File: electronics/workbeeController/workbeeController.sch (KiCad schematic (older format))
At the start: 90 parts, among them J1 24V, J10 LIMIT Y2, J11 LIMIT Z, J12 ESTOP, J13 IN A, J14 IN B, J15 IN C, J16 IN D, J17 PROBE, J18 OUT_A, J19 OUT_B, J2 SR_OUT_EXT, J20 OUT_C, J21 OUT_D, J22 OUT_E, J23 OUT_F, J24 OUT_G, J25 OUT_H, J26 OUT_I, J27 OUT_J, J28 OUT_K, J29 OUT_L, J3 SR_IN_EXT, J30 OUT_M, J31 OUT_N, J32 OUT_O, J33 OUT_P, J34 RS485, J4 Conn_01x03_Male, J5 GND, J6 3.3v, J7 IN, J8 LIMIT X, J9 LIMIT Y1, U1 74HC595, U10 PC817, U11 PC817, U12 PC817, U13 PC817, U14 PC817, U15 PC817, U16 PC817, U2 74HC595, U3 TTGO_TDisplay, U4 Buck, U5 74HC165, U6 SP3485EN, U7 PC817, U8 PC817, U9 PC817

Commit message: Schematic updates
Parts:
- removed J4: Conn_01x03_Male, symbol Connector:Conn_01x03_Male
- added C?: 100uF, symbol Device:CP_Small
- added D?: 24V (Yellow), symbol Device:LED_Small
- added D?: 5V (Blue), symbol Device:LED_Small
- added D?: 3.3V (Green), symbol Device:LED_Small
- added J4: PULSE, symbol Connector:Screw_Terminal_01x03
- added R?: 2.2k, symbol Device:R_Small
- added R? (x2): 220, symbol Device:R_Small
- added U17: LevelShifterModule, symbol LevelShifterModule:LevelShifterModule
- U6: value SP3485EN -> SP485EN
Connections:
- net +24V: now also D?.2 (A)
- net +3V3: now also D?.2 (A), U17.3 (LV); no longer C4.2, R30.1, U6.8 (VCC)
- net +5V: now also C4.2, R30.1, U6.8 (VCC), C?.1, D?.2 (A), J4.2 (Pin_2), U17.10 (HV)
- net GND: now also C?.2, J4.3 (Pin_3), R?.2, R?.2, R?.2, U17.4 (GND), U17.9 (GND)
- net INT_PROBE: now also U3.23 (GPIO36); no longer U3.15 (GPIO27)
- net RS485_DI: now also U17.11 (HV2); no longer U3.19 (GPIO32)
- net RS485_RO: now also U17.12 (HV1); no longer U3.20 (GPIO39)
- net RS485_RTS: now also U17.8 (HV3); no longer U3.18 (GPIO33)
- net SR_IN_LATCH: now also U3.15 (GPIO27); no longer U3.23 (GPIO36)
- net PULSE renamed INT_PULSE
- net INT_PULSE: now also U17.6 (LV4)
- new net: D?.1 (K), R?.1 (x3)
- new net EXT_PULSE: J4.1 (Pin_1), U17.7 (HV4)
- new net RS485_DI_3V3: U17.2 (LV2), U3.19 (GPIO32)
- new net RS485_RO_3V3: U17.1 (LV1), U3.20 (GPIO39)
- new net RS485_RTS_3V3: U17.5 (LV3), U3.18 (GPIO33)
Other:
- note added: "Power"
- moved on the sheet: C3, C4, D1, F1, J1, J3, J34, JP1, R30, R31, R32, U3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

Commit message: Initial schematic and footprints complete
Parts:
- added H1, H2, H3, H4, H5: MountingHole_Pad, MountingHole:MountingHole_4.3mm_M4_ISO7380_Pad, symbol Mechanical:MountingHole_Pad
- added J35: 24V, Connector_PinHeader_2.54mm:PinHeader_1x04_P2.54mm_Vertical, symbol Connector:Conn_01x04_Female
- added J36: 5V, Connector_PinHeader_2.54mm:PinHeader_1x04_P2.54mm_Vertical, symbol Connector:Conn_01x04_Female
- added J37: 3.3V, Connector_PinHeader_2.54mm:PinHeader_1x04_P2.54mm_Vertical, symbol Connector:Conn_01x04_Female
- added J38: GND, Connector_PinHeader_2.54mm:PinHeader_1x04_P2.54mm_Vertical, symbol Connector:Conn_01x04_Female
- C1, C2, C3, C4: footprint (none) -> Capacitor_THT:C_Disc_D5.0mm_W2.5mm_P2.50mm
- C5: renamed from C?; footprint (none) -> Capacitor_THT:CP_Radial_D8.0mm_P3.50mm
- D1, D2: footprint (none) -> Diode_THT:D_DO-41_SOD81_P7.62mm_Horizontal
- D3, D4, D5: renamed from D?; footprint (none) -> LED_THT:LED_D3.0mm
- F1: footprint (none) -> Fuse:Fuse_1206_3216Metric_Pad1.42x1.75mm_HandSolder
- J1, J17, J18, J19, J20, J21, J22, J23, J24, J25, J26, J27, J28, J29, J30, J31, J32, J33: footprint (none) -> ScrewTerminal:057-EB21A-02-D
- J10: value LIMIT Y2 -> IN C; footprint (none) -> ScrewTerminal:057-EB21A-02-D
- J11: value LIMIT Z -> IN D; footprint (none) -> ScrewTerminal:057-EB21A-02-D
- J12: value ESTOP -> IN E; footprint (none) -> ScrewTerminal:057-EB21A-02-D
- J13: value IN A -> IN F; footprint (none) -> ScrewTerminal:057-EB21A-02-D
- J14: value IN B -> IN G; footprint (none) -> ScrewTerminal:057-EB21A-02-D
- J15: value IN C -> IN H; footprint (none) -> ScrewTerminal:057-EB21A-02-D
- J16: value IN D -> ESTOP; footprint (none) -> ScrewTerminal:057-EB21A-02-D
- J2, J3: footprint (none) -> Connector_PinHeader_2.54mm:PinHeader_1x05_P2.54mm_Vertical
- J34: footprint (none) -> RS485:RS485Module
- J4: footprint (none) -> Connector_PinHeader_2.54mm:PinHeader_1x03_P2.54mm_Vertical; symbol Connector:Screw_Terminal_01x03 -> Connector:Conn_01x03_Male
- J5, J6: footprint (none) -> Connector_PinHeader_2.54mm:PinHeader_1x04_P2.54mm_Vertical
- J7: value IN -> GPIO; footprint (none) -> Connector_PinHeader_2.54mm:PinHeader_1x04_P2.54mm_Vertical
- J8: value LIMIT X -> IN A; footprint (none) -> ScrewTerminal:057-EB21A-02-D
- J9: value LIMIT Y1 -> IN B; footprint (none) -> ScrewTerminal:057-EB21A-02-D
- JP1: footprint (none) -> Jumper:SolderJumper-2_P1.3mm_Bridged_Pad1.0x1.5mm
- R1, R10, R11, R12, R13, R14, R15, R16, R17, R18, R19, R2, R20, R21, R22, R23, R24, R25, R26, R27, R28, R29, R3, R30, R31, R32, R4, R5, R6, R7, R8, R9: footprint (none) -> Resistor_THT:R_Axial_DIN0207_L6.3mm_D2.5mm_P7.62mm_Horizontal
- R33, R34, R35: renamed from R?; footprint (none) -> Resistor_THT:R_Axial_DIN0207_L6.3mm_D2.5mm_P7.62mm_Horizontal
- U1, U2: footprint (none) -> Package_DIP:DIP-16_W7.62mm
- U17: footprint (none) -> LevelShifterModule:LevelShifterModule
- U3: footprint (none) -> ESP32:T-DISPLAY
- U4: footprint (none) -> Buck:BuckModule
- U5: footprint MODULE -> Package_DIP:DIP-16_W7.62mm
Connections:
- net EXT_LIMIT_X is gone; now on net EXT_IN_A: J8.2 (Pin_2), U7.1
- net EXT_LIMIT_Y1 is gone; now on net EXT_IN_B: J9.2 (Pin_2), U8.1
- net EXT_LIMIT_Y2 is gone; now on net EXT_IN_C: J10.2 (Pin_2), U9.1
- net EXT_LIMIT_Z is gone; now on net EXT_IN_D: J11.2 (Pin_2), U10.1
- net +24V: now also J35.1 (Pin_1), J35.2 (Pin_2), J35.3 (Pin_3), J35.4 (Pin_4)
- net +3V3: now also J37.1 (Pin_1), J37.2 (Pin_2), J37.3 (Pin_3), J37.4 (Pin_4)
- net +5V: now also J36.1 (Pin_1), J36.2 (Pin_2), J36.3 (Pin_3), J36.4 (Pin_4)
- net EXT_ESTOP: now also J16.2 (Pin_2); no longer J12.2 (Pin_2)
- net EXT_IN_A: no longer J13.2 (Pin_2), U12.1
- net EXT_IN_B: no longer J14.2 (Pin_2), U13.1
- net EXT_IN_C: no longer J15.2 (Pin_2), U14.1
- net EXT_IN_D: no longer J16.2 (Pin_2), U15.1
- net GND: now also J38.1 (Pin_1), J38.2 (Pin_2), J38.3 (Pin_3), J38.4 (Pin_4)
- net INT_IN_A: now also R11.1, U7.4; no longer R16.1, U12.4
- net INT_IN_B: now also R12.1, U8.4; no longer R17.1, U13.4
- net INT_IN_C: now also R13.1, U9.4; no longer R18.1, U14.4
- net INT_IN_D: now also R14.1, U10.4; no longer R19.1, U15.4
- net INT_IN_E: now also R16.1, U12.4; no longer J7.1 (Pin_1)
- net INT_IN_F: now also R17.1, U13.4; no longer J7.2 (Pin_2)
- net INT_IN_G: now also R18.1, U14.4; no longer J7.3 (Pin_3)
- net INT_IN_H: now also R19.1, U15.4; no longer J7.4 (Pin_4)
- removed net INT_LIMIT_X: R11.1, U3.5 (GPIO17), U7.4
- removed net INT_LIMIT_Y1: R12.1, U3.3 (GPIO21), U8.4
- removed net INT_LIMIT_Y2: R13.1, U3.4 (GPIO22), U9.4
- removed net INT_LIMIT_Z: R14.1, U10.4, U3.6 (GPIO2)
- new net EXT_IN_E: J12.2 (Pin_2), U12.1
- new net EXT_IN_F: J13.2 (Pin_2), U13.1
- new net EXT_IN_G: J14.2 (Pin_2), U14.1
- new net EXT_IN_H: J15.2 (Pin_2), U15.1
- new net Earth_Protective: H1.1, H2.1, H3.1, H4.1, H5.1
- new net GPIO_17: J7.2 (Pin_2), U3.5 (GPIO17)
- new net GPIO_2: J7.1 (Pin_1), U3.6 (GPIO2)
- new net GPIO_21: J7.4 (Pin_4), U3.3 (GPIO21)
- new net GPIO_22: J7.3 (Pin_3), U3.4 (GPIO22)
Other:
- note added: "24V input connections"
- note added: "24V isolation"
- note added: "Accessory power"
- note added: "I/O Shift Registers"
- note added: "Input"
- note added: "LEDs"
- note added: "Low voltage I/O connections"
- note added: "MCU"
- note added: "Mechanical"
- note added: "Output"
- note added: "RS485 / 5V interface"
- moved on the sheet: C1, C2, C4, D3, D4, D5, J10, J11, J12, J13, J14, J15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

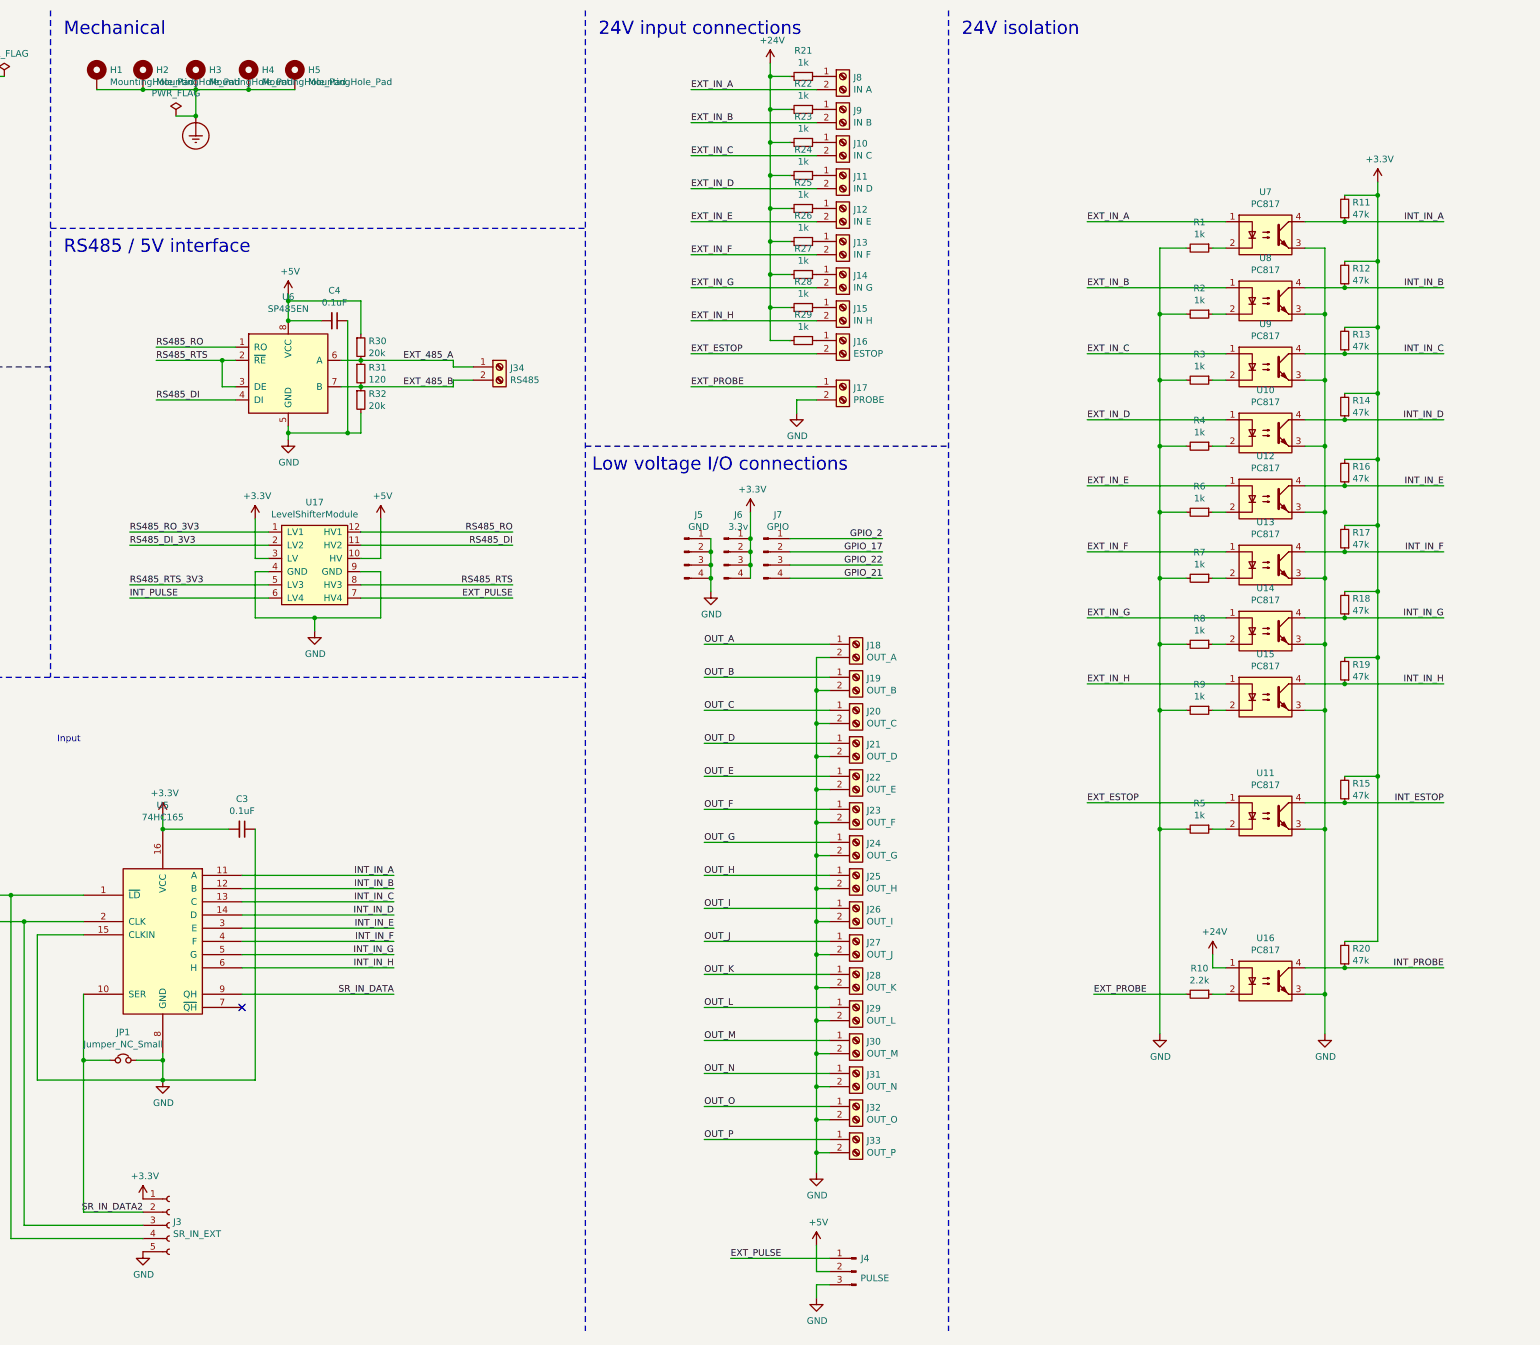
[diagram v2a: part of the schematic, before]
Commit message: Change to pin headers, start PCB
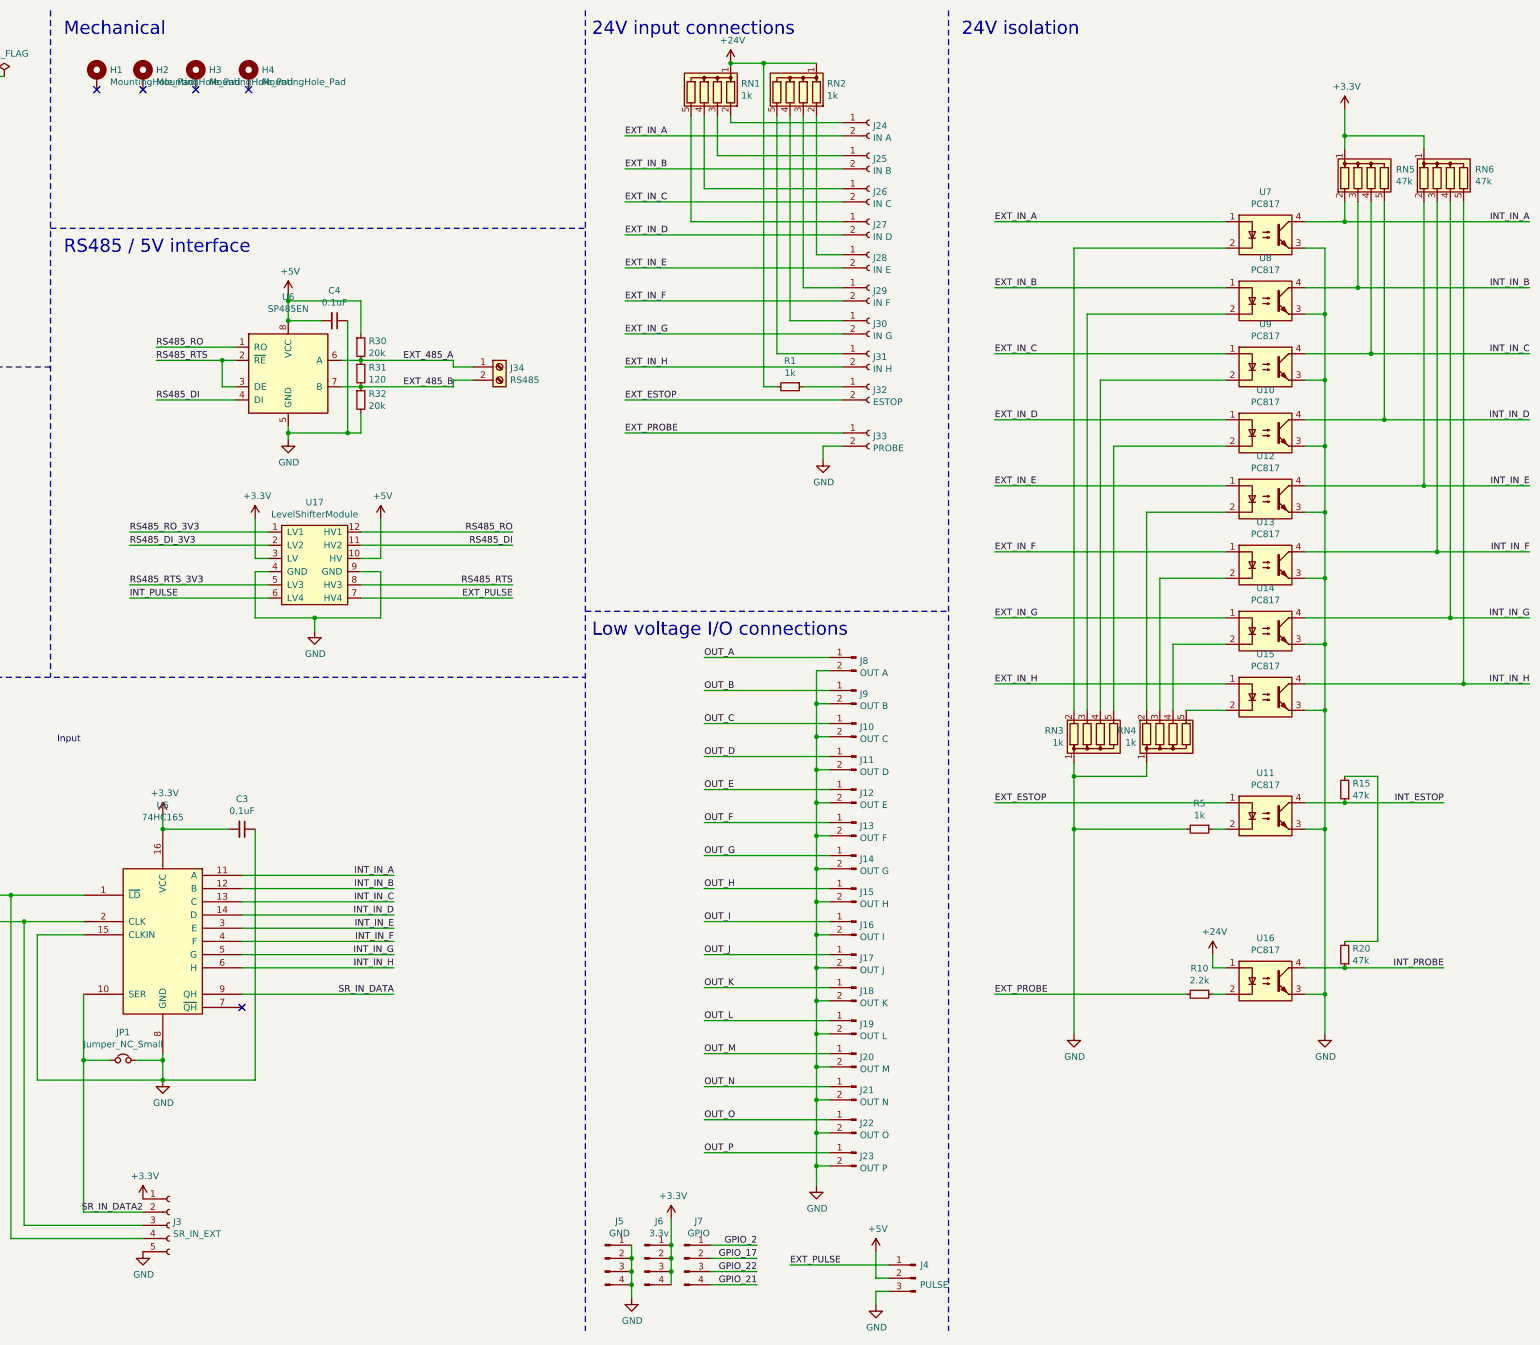
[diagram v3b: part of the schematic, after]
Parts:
- removed H5: MountingHole_Pad, MountingHole:MountingHole_4.3mm_M4_ISO7380_Pad, symbol Mechanical:MountingHole_Pad
- removed J10: IN C, ScrewTerminal:057-EB21A-02-D, symbol Connector:Screw_Terminal_01x02
- removed J11: IN D, ScrewTerminal:057-EB21A-02-D, symbol Connector:Screw_Terminal_01x02
- removed J12: IN E, ScrewTerminal:057-EB21A-02-D, symbol Connector:Screw_Terminal_01x02
- removed J13: IN F, ScrewTerminal:057-EB21A-02-D, symbol Connector:Screw_Terminal_01x02
- removed J14: IN G, ScrewTerminal:057-EB21A-02-D, symbol Connector:Screw_Terminal_01x02
- removed J15: IN H, ScrewTerminal:057-EB21A-02-D, symbol Connector:Screw_Terminal_01x02
- removed J16: ESTOP, ScrewTerminal:057-EB21A-02-D, symbol Connector:Screw_Terminal_01x02
- removed J17: PROBE, ScrewTerminal:057-EB21A-02-D, symbol Connector:Screw_Terminal_01x02
- removed J18: OUT_A, ScrewTerminal:057-EB21A-02-D, symbol Connector:Screw_Terminal_01x02
- removed J19: OUT_B, ScrewTerminal:057-EB21A-02-D, symbol Connector:Screw_Terminal_01x02
- removed J20: OUT_C, ScrewTerminal:057-EB21A-02-D, symbol Connector:Screw_Terminal_01x02
- removed J21: OUT_D, ScrewTerminal:057-EB21A-02-D, symbol Connector:Screw_Terminal_01x02
- removed J22: OUT_E, ScrewTerminal:057-EB21A-02-D, symbol Connector:Screw_Terminal_01x02
- removed J23: OUT_F, ScrewTerminal:057-EB21A-02-D, symbol Connector:Screw_Terminal_01x02
- removed J24: OUT_G, ScrewTerminal:057-EB21A-02-D, symbol Connector:Screw_Terminal_01x02
- removed J25: OUT_H, ScrewTerminal:057-EB21A-02-D, symbol Connector:Screw_Terminal_01x02
- removed J26: OUT_I, ScrewTerminal:057-EB21A-02-D, symbol Connector:Screw_Terminal_01x02
- removed J27: OUT_J, ScrewTerminal:057-EB21A-02-D, symbol Connector:Screw_Terminal_01x02
- removed J28: OUT_K, ScrewTerminal:057-EB21A-02-D, symbol Connector:Screw_Terminal_01x02
- removed J29: OUT_L, ScrewTerminal:057-EB21A-02-D, symbol Connector:Screw_Terminal_01x02
- removed J30: OUT_M, ScrewTerminal:057-EB21A-02-D, symbol Connector:Screw_Terminal_01x02
- removed J31: OUT_N, ScrewTerminal:057-EB21A-02-D, symbol Connector:Screw_Terminal_01x02
- removed J32: OUT_O, ScrewTerminal:057-EB21A-02-D, symbol Connector:Screw_Terminal_01x02
- removed J33: OUT_P, ScrewTerminal:057-EB21A-02-D, symbol Connector:Screw_Terminal_01x02
- removed J8: IN A, ScrewTerminal:057-EB21A-02-D, symbol Connector:Screw_Terminal_01x02
- removed J9: IN B, ScrewTerminal:057-EB21A-02-D, symbol Connector:Screw_Terminal_01x02
- removed R11, R12, R13, R14, R16, R17, R18, R19: 47k, Resistor_THT:R_Axial_DIN0207_L6.3mm_D2.5mm_P7.62mm_Horizontal, symbol Device:R_Small
- removed R2, R21, R22, R23, R24, R25, R26, R27, R28, R29, R3, R4, R6, R7, R8, R9: 1k, Resistor_THT:R_Axial_DIN0207_L6.3mm_D2.5mm_P7.62mm_Horizontal, symbol Device:R_Small
- added J10: OUT C, Connector_PinHeader_2.54mm:PinHeader_1x02_P2.54mm_Vertical, symbol Connector:Conn_01x02_Male
- added J11: OUT D, Connector_PinHeader_2.54mm:PinHeader_1x02_P2.54mm_Vertical, symbol Connector:Conn_01x02_Male
- added J12: OUT E, Connector_PinHeader_2.54mm:PinHeader_1x02_P2.54mm_Vertical, symbol Connector:Conn_01x02_Male
- added J13: OUT F, Connector_PinHeader_2.54mm:PinHeader_1x02_P2.54mm_Vertical, symbol Connector:Conn_01x02_Male
- added J14: OUT G, Connector_PinHeader_2.54mm:PinHeader_1x02_P2.54mm_Vertical, symbol Connector:Conn_01x02_Male
- added J15: OUT H, Connector_PinHeader_2.54mm:PinHeader_1x02_P2.54mm_Vertical, symbol Connector:Conn_01x02_Male
- added J16: OUT I, Connector_PinHeader_2.54mm:PinHeader_1x02_P2.54mm_Vertical, symbol Connector:Conn_01x02_Male
- added J17: OUT J, Connector_PinHeader_2.54mm:PinHeader_1x02_P2.54mm_Vertical, symbol Connector:Conn_01x02_Male
- added J18: OUT K, Connector_PinHeader_2.54mm:PinHeader_1x02_P2.54mm_Vertical, symbol Connector:Conn_01x02_Male
- added J19: OUT L, Connector_PinHeader_2.54mm:PinHeader_1x02_P2.54mm_Vertical, symbol Connector:Conn_01x02_Male
- added J20: OUT M, Connector_PinHeader_2.54mm:PinHeader_1x02_P2.54mm_Vertical, symbol Connector:Conn_01x02_Male
- added J21: OUT N, Connector_PinHeader_2.54mm:PinHeader_1x02_P2.54mm_Vertical, symbol Connector:Conn_01x02_Male
- added J22: OUT O, Connector_PinHeader_2.54mm:PinHeader_1x02_P2.54mm_Vertical, symbol Connector:Conn_01x02_Male
- added J23: OUT P, Connector_PinHeader_2.54mm:PinHeader_1x02_P2.54mm_Vertical, symbol Connector:Conn_01x02_Male
- added J24: IN A, Connector_PinHeader_2.54mm:PinHeader_1x02_P2.54mm_Vertical, symbol Connector:Conn_01x02_Female
- added J25: IN B, Connector_PinHeader_2.54mm:PinHeader_1x02_P2.54mm_Vertical, symbol Connector:Conn_01x02_Female
- added J26: IN C, Connector_PinHeader_2.54mm:PinHeader_1x02_P2.54mm_Vertical, symbol Connector:Conn_01x02_Female
- added J27: IN D, Connector_PinHeader_2.54mm:PinHeader_1x02_P2.54mm_Vertical, symbol Connector:Conn_01x02_Female
- added J28: IN E, Connector_PinHeader_2.54mm:PinHeader_1x02_P2.54mm_Vertical, symbol Connector:Conn_01x02_Female
- added J29: IN F, Connector_PinHeader_2.54mm:PinHeader_1x02_P2.54mm_Vertical, symbol Connector:Conn_01x02_Female
- added J30: IN G, Connector_PinHeader_2.54mm:PinHeader_1x02_P2.54mm_Vertical, symbol Connector:Conn_01x02_Female
- added J31: IN H, Connector_PinHeader_2.54mm:PinHeader_1x02_P2.54mm_Vertical, symbol Connector:Conn_01x02_Female
- added J32: ESTOP, Connector_PinHeader_2.54mm:PinHeader_1x02_P2.54mm_Vertical, symbol Connector:Conn_01x02_Female
- added J33: PROBE, Connector_PinHeader_2.54mm:PinHeader_1x02_P2.54mm_Vertical, symbol Connector:Conn_01x02_Female
- added J8: OUT A, Connector_PinHeader_2.54mm:PinHeader_1x02_P2.54mm_Vertical, symbol Connector:Conn_01x02_Male
- added J9: OUT B, Connector_PinHeader_2.54mm:PinHeader_1x02_P2.54mm_Vertical, symbol Connector:Conn_01x02_Male
- added RN1, RN2, RN3, RN4: 1k, Resistor_THT:R_Array_SIP5, symbol Device:R_Network04
- added RN5, RN6: 47k, Resistor_THT:R_Array_SIP5, symbol Device:R_Network04
- F1: footprint Fuse:Fuse_1206_3216Metric_Pad1.42x1.75mm_HandSolder -> Capacitor_THT:C_Disc_D10.5mm_W5.0mm_P5.00mm
- J34: footprint RS485:RS485Module -> ScrewTerminal:057-EB21A-02-D
- R1, R10, R15, R20, R30, R31, R32, R33, R34, R35, R5: footprint Resistor_THT:R_Axial_DIN0207_L6.3mm_D2.5mm_P7.62mm_Horizontal -> Resistor_THT:R_Axial_DIN0207_L6.3mm_D2.5mm_P2.54mm_Vertical
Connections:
- net +24V: now also R1.2, RN1.1 (common), RN2.1 (common)
- net +3V3: now also RN5.1 (common), RN6.1 (common); no longer R15.2, R20.2
- net EXT_ESTOP: now also J32.2 (Pin_2)
- net EXT_IN_A: now also J24.2 (Pin_2)
- net EXT_IN_B: now also J25.2 (Pin_2)
- net EXT_IN_C: now also J26.2 (Pin_2)
- net EXT_IN_D: now also J27.2 (Pin_2)
- net EXT_IN_E: now also J28.2 (Pin_2)
- net EXT_IN_F: now also J29.2 (Pin_2)
- net EXT_IN_G: now also J30.2 (Pin_2)
- net EXT_IN_H: now also J31.2 (Pin_2)
- net EXT_PROBE: now also J33.1 (Pin_1)
- net GND: now also J10.2 (Pin_2), J11.2 (Pin_2), J12.2 (Pin_2), J13.2 (Pin_2), J14.2 (Pin_2), J15.2 (Pin_2), J16.2 (Pin_2), J17.2 (Pin_2), J18.2 (Pin_2), J19.2 (Pin_2), J20.2 (Pin_2), J21.2 (Pin_2), J22.2 (Pin_2), J23.2 (Pin_2), J33.2 (Pin_2), J8.2 (Pin_2), J9.2 (Pin_2), RN3.1 (common), RN4.1 (common); no longer R1.2
- net INT_IN_A: now also RN5.2 (R1)
- net INT_IN_B: now also RN5.3 (R2)
- net INT_IN_C: now also RN5.4 (R3)
- net INT_IN_D: now also RN5.5 (R4)
- net INT_IN_E: now also RN6.2 (R1)
- net INT_IN_F: now also RN6.3 (R2)
- net INT_IN_G: now also RN6.4 (R3)
- net INT_IN_H: now also RN6.5 (R4)
- net OUT_A: now also J8.1 (Pin_1)
- net OUT_B: now also J9.1 (Pin_1)
- net OUT_C: now also J10.1 (Pin_1)
- net OUT_D: now also J11.1 (Pin_1)
- net OUT_E: now also J12.1 (Pin_1)
- net OUT_F: now also J13.1 (Pin_1)
- net OUT_G: now also J14.1 (Pin_1)
- net OUT_H: now also J15.1 (Pin_1)
- net OUT_I: now also J16.1 (Pin_1)
- net OUT_J: now also J17.1 (Pin_1)
- net OUT_K: now also J18.1 (Pin_1)
- net OUT_L: now also J19.1 (Pin_1)
- net OUT_M: now also J20.1 (Pin_1)
- net OUT_N: now also J21.1 (Pin_1)
- net OUT_O: now also J22.1 (Pin_1)
- net OUT_P: now also J23.1 (Pin_1)
- net at U7.2: now also RN3.2 (R1); no longer R1.1
- net at U8.2: now also RN3.3 (R2)
- net at U9.2: now also RN3.4 (R3)
- net at U10.2: now also RN3.5 (R4)
- net at U12.2: now also RN4.2 (R1)
- net at U13.2: now also RN4.3 (R2)
- net at U14.2: now also RN4.4 (R3)
- net at U15.2: now also RN4.5 (R4)
- removed net Earth_Protective: H1.1, H2.1, H3.1, H4.1
- new net: R15.2, R20.2
- new net: J24.1 (Pin_1), RN1.2 (R1)
- new net: J25.1 (Pin_1), RN1.3 (R2)
- new net: J26.1 (Pin_1), RN1.4 (R3)
- new net: J27.1 (Pin_1), RN1.5 (R4)
- new net: J28.1 (Pin_1), RN2.2 (R1)
- new net: J29.1 (Pin_1), RN2.3 (R2)
- new net: J30.1 (Pin_1), RN2.4 (R3)
- new net: J31.1 (Pin_1), RN2.5 (R4)
- new net: J32.1 (Pin_1), R1.1
- no-connect marks 1 -> 5
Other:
- moved on the sheet: J4, J5, J6, J7
